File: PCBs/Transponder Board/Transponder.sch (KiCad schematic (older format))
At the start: 16 parts

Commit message: fixed swapped pins
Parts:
- added U?: PI4ULS5V201TAEX, symbol PI4ULS5V201TAEX
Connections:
- net XBEE-DIN: now also A?.1 (D0/TX)
- net XBEE-DOUT: now also U?.6 (B)
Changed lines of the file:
@@
+	1    0    0    -1
+$EndComp
+Text GLabel 4050 2650 2    60   Input ~ 0
+XBEE-DIN
+Text GLabel 6400 2950 2    60   Input ~ 0
+XBEE-DOUT
+$Comp
+L PI4ULS5V201TAEX U?
+U 1 1 5AB6D5A2
+P 5950 3100
+F 0 "U?" H 5950 3650 60  0000 C CNN
+F 1 "PI4ULS5V201TAEX" H 5950 3000 60  0000 C CNN
+F 2 "" H 5950 3100 60  0001 C CNN
+F 3 "" H 5950 3100 60  0001 C CNN
+	1    5950 3100
 	1    0    0    -1
 $EndComp

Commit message: transponder board
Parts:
- added J?: Conn_01x09, symbol Conn_01x09
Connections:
- net 5V: now also U?.1 (VccA), J?.2 (Pin_2)
- net D2: now also A?.9 (D6); no longer A?.5 (D2)
- net D3: now also A?.10 (D7); no longer A?.6 (D3)
- net D4: now also A?.11 (D8); no longer A?.7 (D4)
- net GND: now also U?.4 (GND), J?.1 (Pin_1), J?.4 (Pin_4)
- net MISO: now also J?.3 (Pin_3)
- net MOSI: now also J?.5 (Pin_5)
- net at A?.2 (D1/RX): now also U?.2 (A)
- net LCD_D4: now reaches A?.8 (D5)
- net LCD_D4: now also J?.6 (Pin_6)
- net 3.3V: now reaches C2.1, U?.1 (Vcc), U?.3 (+Vout)
- net 3.3V: now also U?.5 (EN), U?.8 (VccB)
- new net LCD_D5: A?.7 (D4), J?.7 (Pin_7)
- new net LCD_D6: A?.6 (D3), J?.8 (Pin_8)
- new net LCD_D7: A?.5 (D2), J?.9 (Pin_9)
- no-connect marks 0 -> 2
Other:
- note added: "LCD Pin 1"
- note added: "LCD Pin 2"
- note added: "LCD pin 11"
- note added: "LCD pin 12"
- note added: "LCD pin 13"
- note added: "LCD pin 14"
- note added: "LCD pin 4"
- note added: "LCD pin 5"
- note added: "LCD pin 6"
- moved on the sheet: A?, C1, C2, R1, R2, R?, U?

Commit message: transponder board
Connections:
- net D2: now also A?.19 (AD0/D14); no longer A?.9 (D6)
- net D3: now also A?.20 (AD1/D15); no longer A?.10 (D7)
- net D4: now also A?.21 (AD2/D16); no longer A?.11 (D8)
- net MISO: no longer J?.3 (Pin_3)
- net MOSI: no longer J?.5 (Pin_5)
- new net LCD_H/L_EN: A?.9 (D6), J?.5 (Pin_5)
- new net LCD_H/L_RS: A?.10 (D7), J?.3 (Pin_3)
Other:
- moved on the sheet: R?
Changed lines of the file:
@@
 Text GLabel 1550 3250 2    60   Input ~ 0
 5V
-Text GLabel 3650 4600 2    60   Input ~ 0
+Text GLabel 3650 5400 2    60   Input ~ 0
 D2
-Text GLabel 3350 4700 2    60   Input ~ 0
+Text GLabel 3350 5500 2    60   Input ~ 0
 D3
-Text GLabel 3050 4800 2    60   Input ~ 0
+Text GLabel 3050 5600 2    60   Input ~ 0
 D4
 Text GLabel 1550 2500 2    60   Input ~ 0
@@
 L R R?
 U 1 1 5AA8AA2D
-P 3300 4850
-F 0 "R?" V 3400 4850 50  0000 C CNN
-F 1 "10k" V 3300 4850 50  0000 C CNN
-F 2 "" V 3230 4850 50  0001 C CNN
-F 3 "" H 3300 4850 50  0001 C CNN
-	1    3300 4850
+P 3300 5650
+F 0 "R?" V 3400 5650 50  0000 C CNN
+F 1 "10k" V 3300 5650 50  0000 C CNN
+F 2 "" V 3230 5650 50  0001 C CNN
+F 3 "" H 3300 5650 50  0001 C CNN
+	1    3300 5650
 	1    0    0    -1
 $EndComp
@@
 L R R?
 U 1 1 5AA8AB66
-P 3000 4950
-F 0 "R?" V 3100 4950 50  0000 C CNN
-F 1 "10k" V 3000 4950 50  0000 C CNN
-F 2 "" V 2930 4950 50  0001 C CNN
-F 3 "" H 3000 4950 50  0001 C CNN
-	1    3000 4950
+P 3000 5750
+F 0 "R?" V 3100 5750 50  0000 C CNN
+F 1 "10k" V 3000 5750 50  0000 C CNN
+F 2 "" V 2930 5750 50  0001 C CNN
+F 3 "" H 3000 5750 50  0001 C CNN
+	1    3000 5750
 	1    0    0    -1
 $EndComp
@@
 L R R?
 U 1 1 5AA8A8A4
-P 3600 4750
-F 0 "R?" V 3680 4750 50  0000 C CNN
-F 1 "10k" V 3600 4750 50  0000 C CNN
-F 2 "" V 3530 4750 50  0001 C CNN
-F 3 "" H 3600 4750 50  0001 C CNN
-	1    3600 4750
-	1    0    0    -1
-$EndComp
-Wire Wire Line
-	2600 4600 3600 4600
-Wire Wire Line
-	3600 4600 3650 4600
-Connection ~ 3600 4600
-Wire Wire Line
-	2600 4700 3300 4700
-Wire Wire Line
-	3300 4700 3350 4700
-Connection ~ 3300 4700
-Wire Wire Line
-	2600 4800 3000 4800
-Wire Wire Line
-	3000 4800 3050 4800
-Connection ~ 3000 4800
+P 3600 5550
+F 0 "R?" V 3680 5550 50  0000 C CNN
+F 1 "10k" V 3600 5550 50  0000 C CNN
+F 2 "" V 3530 5550 50  0001 C CNN
+F 3 "" H 3600 5550 50  0001 C CNN
+	1    3600 5550
+	1    0    0    -1
+$EndComp
+Wire Wire Line
+	2600 5400 3600 5400
+Wire Wire Line
+	3600 5400 3650 5400
+Connection ~ 3600 5400
+Wire Wire Line
+	2600 5500 3300 5500
+Wire Wire Line
+	3300 5500 3350 5500
+Connection ~ 3300 5500
+Wire Wire Line
+	2600 5600 3000 5600
+Wire Wire Line
+	3000 5600 3050 5600
+Connection ~ 3000 5600
 $Comp
 L GND #PWR?
 U 1 1 5AA8AFB2
-P 3000 5100
-F 0 "#PWR?" H 3000 4850 50  0001 C CNN
-F 1 "GND" H 3000 4950 50  0000 C CNN
-F 2 "" H 3000 5100 50  0001 C CNN
-F 3 "" H 3000 5100 50  0001 C CNN
-	1    3000 5100
+P 3000 5900
+F 0 "#PWR?" H 3000 5650 50  0001 C CNN
+F 1 "GND" H 3000 5750 50  0000 C CNN
+F 2 "" H 3000 5900 50  0001 C CNN
+F 3 "" H 3000 5900 50  0001 C CNN
+	1    3000 5900
 	1    0    0    -1
 $EndComp
@@
 L GND #PWR?
 U 1 1 5AA8AFED
-P 3300 5000
-F 0 "#PWR?" H 3300 4750 50  0001 C CNN
-F 1 "GND" H 3300 4850 50  0000 C CNN
-F 2 "" H 3300 5000 50  0001 C CNN
-F 3 "" H 3300 5000 50  0001 C CNN
-	1    3300 5000
+P 3300 5800
+F 0 "#PWR?" H 3300 5550 50  0001 C CNN
+F 1 "GND" H 3300 5650 50  0000 C CNN
+F 2 "" H 3300 5800 50  0001 C CNN
+F 3 "" H 3300 5800 50  0001 C CNN
+	1    3300 5800
 	1    0    0    -1
 $EndComp
@@
 L GND #PWR?
 U 1 1 5AA8B028
-P 3600 4900
-F 0 "#PWR?" H 3600 4650 50  0001 C CNN
-F 1 "GND" H 3600 4750 50  0000 C CNN
-F 2 "" H 3600 4900 50  0001 C CNN
-F 3 "" H 3600 4900 50  0001 C CNN
-	1    3600 4900
+P 3600 5700
+F 0 "#PWR?" H 3600 5450 50  0001 C CNN
+F 1 "GND" H 3600 5550 50  0000 C CNN
+F 2 "" H 3600 5700 50  0001 C CNN
+F 3 "" H 3600 5700 50  0001 C CNN
+	1    3600 5700
 	1    0    0    -1
 $EndComp
@@
 L GND #PWR?
 U 1 1 5AB72A73
-P 5500 5900
-F 0 "#PWR?" H 5500 5650 50  0001 C CNN
-F 1 "GND" H 5500 5750 50  0000 C CNN
-F 2 "" H 5500 5900 50  0001 C CNN
-F 3 "" H 5500 5900 50  0001 C CNN
-	1    5500 5900
-	1    0    0    -1
-$EndComp
-Wire Wire Line
-	5500 5900 5500 5550
-Wire Wire Line
-	5500 5550 5950 5550
+P 5300 5900
+F 0 "#PWR?" H 5300 5650 50  0001 C CNN
+F 1 "GND" H 5300 5750 50  0000 C CNN
+F 2 "" H 5300 5900 50  0001 C CNN
+F 3 "" H 5300 5900 50  0001 C CNN
+	1    5300 5900
+	1    0    0    -1
+$EndComp
+Wire Wire Line
+	5300 5900 5300 5550
+Wire Wire Line
+	5300 5550 5950 5550
 Text GLabel 5950 5350 0    60   Input ~ 0
 LCD_D4
@@
 Text Notes 6750 5100 2    60   ~ 0
 LCD pin 14
-Text GLabel 5950 5450 0    60   Input ~ 0
-MOSI
-Text GLabel 5950 5650 0    60   Input ~ 0
-MISO
 Text GLabel 2600 4500 2    60   Input ~ 0
 LCD_D4
@@
 Text GLabel 2600 4200 2    60   Input ~ 0
 LCD_D7
+Text GLabel 5950 5450 0    60   Input ~ 0
+LCD_H/L_EN
+Text GLabel 5950 5650 0    60   Input ~ 0
+LCD_H/L_RS
+Text GLabel 2600 4600 2    60   Input ~ 0
+LCD_H/L_EN
+Text GLabel 2600 4700 2    60   Input ~ 0
+LCD_H/L_RS
 $EndSCHEMATC

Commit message: pinout changes
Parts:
- removed U?: PI4ULS5V201TAEX, symbol PI4ULS5V201TAEX
- added C?: 8.2pF, symbol C
- added C?: 1uF, symbol C
- added C?: 10uF, symbol C
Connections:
- net 3.3V: now also C?.1, C?.1, C?.1
- net GND: now also C?.2, C?.2, C?.2
- net shifter/A: now reaches A?.2 (D1/RX)
- net BATT+: no longer names the net of J?.1 (Pin_1), J?.2 (Pin_2)
- no-connect marks 2 -> 0
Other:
- note added: "Battery"
- note added: "Switch"
- moved on the sheet: J?, R1, R2, U?
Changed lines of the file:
@@
 $Descr A4 11693 8268
 encoding utf-8
-Sheet 1 1
+Sheet 1 2
 Title ""
 Date ""
@@
 L XBee-S2C U?
 U 1 1 5AA887F8
-P 6650 2200
-F 0 "U?" H 6550 3000 60  0000 C CNN
-F 1 "XBee-S2C" H 6650 1400 60  0000 C CNN
-F 2 "" H 6250 2150 60  0001 C CNN
-F 3 "" H 6250 2150 60  0001 C CNN
-	1    6650 2200
+P 9000 2250
+F 0 "U?" H 8900 3050 60  0000 C CNN
+F 1 "XBee-S2C" H 9000 1450 60  0000 C CNN
+F 2 "" H 8600 2200 60  0001 C CNN
+F 3 "" H 8600 2200 60  0001 C CNN
+	1    9000 2250
 	1    0    0    -1
 $EndComp
@@
 Wire Wire Line
 	5150 1350 5150 1250
-Text GLabel 5550 1850 0    60   Input ~ 0
+Text GLabel 7900 1900 0    60   Input ~ 0
 XBEE-DOUT
-Text GLabel 3950 2100 0    60   Input ~ 0
+Text GLabel 6050 2150 0    60   Input ~ 0
 XBEE-DIN
 $Comp
 L R R2
 U 1 1 5AA89647
-P 4100 2600
-F 0 "R2" V 4180 2600 50  0000 C CNN
-F 1 "2k" V 4100 2600 50  0000 C CNN
-F 2 "" V 4030 2600 50  0001 C CNN
-F 3 "" H 4100 2600 50  0001 C CNN
-	1    4100 2600
+P 6300 2650
+F 0 "R2" V 6380 2650 50  0000 C CNN
+F 1 "2k" V 6300 2650 50  0000 C CNN
+F 2 "" V 6230 2650 50  0001 C CNN
+F 3 "" H 6300 2650 50  0001 C CNN
+	1    6300 2650
 	1    0    0    -1
 $EndComp
@@
 L R R1
 U 1 1 5AA8967B
-P 4100 3200
-F 0 "R1" V 4180 3200 50  0000 C CNN
-F 1 "3k" V 4100 3200 50  0000 C CNN
-F 2 "" V 4030 3200 50  0001 C CNN
-F 3 "" H 4100 3200 50  0001 C CNN
-	1    4100 3200
-	1    0    0    -1
-$EndComp
-Wire Wire Line
-	3950 2100 4100 2100
-Wire Wire Line
-	4100 2100 4100 2450
-Wire Wire Line
-	4100 2750 4100 2900
-Wire Wire Line
-	4100 2900 4100 3050
-Wire Wire Line
-	4100 2900 4650 2900
-Wire Wire Line
-	4650 2900 4650 1950
-Wire Wire Line
-	4650 1950 5550 1950
-Connection ~ 4100 2900
+P 6300 3200
+F 0 "R1" V 6380 3200 50  0000 C CNN
+F 1 "3k" V 6300 3200 50  0000 C CNN
+F 2 "" V 6230 3200 50  0001 C CNN
+F 3 "" H 6300 3200 50  0001 C CNN
+	1    6300 3200
+	1    0    0    -1
+$EndComp
+Wire Wire Line
+	6050 2150 6300 2150
+Wire Wire Line
+	6300 2150 6300 2500
+Wire Wire Line
+	6300 2800 6300 2950
+Wire Wire Line
+	6300 2950 6300 3050
+Wire Wire Line
+	6300 2950 7700 2950
+Wire Wire Line
+	7700 2950 7700 2000
+Wire Wire Line
+	7700 2000 7900 2000
+Connection ~ 6300 2950
 $Comp
 L GND #PWR?
 U 1 1 5AA89745
-P 4100 3450
-F 0 "#PWR?" H 4100 3200 50  0001 C CNN
-F 1 "GND" H 4100 3300 50  0000 C CNN
-F 2 "" H 4100 3450 50  0001 C CNN
-F 3 "" H 4100 3450 50  0001 C CNN
-	1    4100 3450
-	1    0    0    -1
-$EndComp
-Wire Wire Line
-	4100 3450 4100 3350
+P 6300 3500
+F 0 "#PWR?" H 6300 3250 50  0001 C CNN
+F 1 "GND" H 6300 3350 50  0000 C CNN
+F 2 "" H 6300 3500 50  0001 C CNN
+F 3 "" H 6300 3500 50  0001 C CNN
+	1    6300 3500
+	1    0    0    -1
+$EndComp
+Wire Wire Line
+	6300 3500 6300 3350
 $Comp
 L GND #PWR?
 U 1 1 5AA897AD
-P 5450 2850
-F 0 "#PWR?" H 5450 2600 50  0001 C CNN
-F 1 "GND" H 5450 2700 50  0000 C CNN
-F 2 "" H 5450 2850 50  0001 C CNN
-F 3 "" H 5450 2850 50  0001 C CNN
-	1    5450 2850
-	1    0    0    -1
-$EndComp
-Wire Wire Line
-	5450 2850 5450 2650
-Wire Wire Line
-	5450 2650 5550 2650
-Text GLabel 1550 1950 2    60   Input ~ 0
+P 7800 2900
+F 0 "#PWR?" H 7800 2650 50  0001 C CNN
+F 1 "GND" H 7800 2750 50  0000 C CNN
+F 2 "" H 7800 2900 50  0001 C CNN
+F 3 "" H 7800 2900 50  0001 C CNN
+	1    7800 2900
+	1    0    0    -1
+$EndComp
+Wire Wire Line
+	7800 2900 7800 2700
+Wire Wire Line
+	7800 2700 7900 2700
+Text GLabel 1550 1700 2    60   Input ~ 0
 7.4V
-Text GLabel 1550 1850 2    60   Input ~ 0
-BATT+
-Text GLabel 1550 1100 2    60   Input ~ 0
-BATT+
 $Comp
 L GND #PWR?
@@
 L Conn_01x02 J?
 U 1 1 5AA8A05F
-P 1350 1950
-F 0 "J?" H 1350 2050 50  0000 C CNN
-F 1 "Conn_01x02" H 1350 1750 50  0000 C CNN
-F 2 "" H 1350 1950 50  0001 C CNN
-F 3 "" H 1350 1950 50  0001 C CNN
-	1    1350 1950
+P 1350 1700
+F 0 "J?" H 1350 1800 50  0000 C CNN
+F 1 "Conn_01x02" H 1350 1500 50  0000 C CNN
+F 2 "" H 1350 1700 50  0001 C CNN
+F 3 "" H 1350 1700 50  0001 C CNN
+	1    1350 1700
 	-1   0    0    1
 $EndComp
@@
 Text GLabel 2600 4000 2    60   Input ~ 0
 XBEE-DIN
-Text GLabel 4950 4200 2    60   Input ~ 0
-XBEE-DOUT
-$Comp
-L PI4ULS5V201TAEX U?
-U 1 1 5AB6D5A2
-P 4500 4350
-F 0 "U?" H 4500 4900 60  0000 C CNN
-F 1 "PI4ULS5V201TAEX" H 4500 4250 60  0000 C CNN
-F 2 "" H 4500 4350 60  0001 C CNN
-F 3 "" H 4500 4350 60  0001 C CNN
-	1    4500 4350
-	1    0    0    -1
-$EndComp
 Text GLabel 5500 900  2    60   Input ~ 0
 3.3V
@@
 Wire Wire Line
 	5150 900  5500 900
-Text GLabel 5550 1750 0    60   Input ~ 0
+Text GLabel 6400 1800 0    60   Input ~ 0
 3.3V
-Text GLabel 4950 4000 2    60   Input ~ 0
-3.3V
-Text GLabel 4950 4300 2    60   Input ~ 0
-3.3V
-Wire Wire Line
-	2600 4100 4050 4100
-Text GLabel 4050 4000 0    60   Input ~ 0
-5V
-$Comp
-L GND #PWR?
-U 1 1 5AB70428
-P 3950 4400
-F 0 "#PWR?" H 3950 4150 50  0001 C CNN
-F 1 "GND" H 3950 4250 50  0000 C CNN
-F 2 "" H 3950 4400 50  0001 C CNN
-F 3 "" H 3950 4400 50  0001 C CNN
-	1    3950 4400
-	1    0    0    -1
-$EndComp
-Wire Wire Line
-	3950 4400 3950 4300
-Wire Wire Line
-	3950 4300 4050 4300
-NoConn ~ 4950 4100
-NoConn ~ 4050 4200
 $Comp
 L Conn_01x09 J?
@@
 Text GLabel 2600 4700 2    60   Input ~ 0
 LCD_H/L_RS
+Wire Wire Line
+	1550 1100 1750 1100
+Wire Wire Line
+	1750 1100 1750 1600
+Wire Wire Line
+	1750 1600 1550 1600
+Text Notes 950  1100 0    60   ~ 0
+Battery
+Text Notes 950  1700 0    60   ~ 0
+Switch
+$Comp
+L C C?
+U 1 1 5AB9BB4C
+P 7150 2000
+F 0 "C?" H 7175 2100 50  0000 L CNN
+F 1 "8.2pF" H 7175 1900 50  0000 L CNN
+F 2 "" H 7188 1850 50  0001 C CNN
+F 3 "" H 7150 2000 50  0001 C CNN
+	1    7150 2000
+	1    0    0    -1
+$EndComp
+$Comp
+L C C?
+U 1 1 5AB9BC07
+P 6850 2000
+F 0 "C?" H 6875 2100 50  0000 L CNN
+F 1 "1uF" H 6875 1900 50  0000 L CNN
+F 2 "" H 6888 1850 50  0001 C CNN
+F 3 "" H 6850 2000 50  0001 C CNN
+	1    6850 2000
+	1    0    0    -1
+$EndComp
+$Comp
+L C C?
+U 1 1 5AB9BC5D
+P 6550 2000
+F 0 "C?" H 6575 2100 50  0000 L CNN
+F 1 "10uF" H 6575 1900 50  0000 L CNN
+F 2 "" H 6588 1850 50  0001 C CNN
+F 3 "" H 6550 2000 50  0001 C CNN
+	1    6550 2000
+	1    0    0    -1
+$EndComp
+Wire Wire Line
+	6400 1800 6550 1800
+Wire Wire Line
+	6550 1800 6850 1800
+Wire Wire Line
+	6850 1800 7150 1800
+Wire Wire Line
+	7150 1800 7900 1800
+Wire Wire Line
+	6550 1850 6550 1800
+Connection ~ 6550 1800
+Wire Wire Line
+	6850 1850 6850 1800
+Connection ~ 6850 1800
+Wire Wire Line
+	7150 1850 7150 1800
+Connection ~ 7150 1800
+$Comp
+L GND #PWR?
+U 1 1 5AB9C29E
+P 6550 2150
+F 0 "#PWR?" H 6550 1900 50  0001 C CNN
+F 1 "GND" H 6550 2000 50  0000 C CNN
+F 2 "" H 6550 2150 50  0001 C CNN
+F 3 "" H 6550 2150 50  0001 C CNN
+	1    6550 2150
+	1    0    0    -1
+$EndComp
+$Comp
+L GND #PWR?
+U 1 1 5AB9C2E8
+P 6850 2150
+F 0 "#PWR?" H 6850 1900 50  0001 C CNN
+F 1 "GND" H 6850 2000 50  0000 C CNN
+F 2 "" H 6850 2150 50  0001 C CNN
+F 3 "" H 6850 2150 50  0001 C CNN
+	1    6850 2150
+	1    0    0    -1
+$EndComp
+$Comp
+L GND #PWR?
+U 1 1 5AB9C332
+P 7150 2150
+F 0 "#PWR?" H 7150 1900 50  0001 C CNN
+F 1 "GND" H 7150 2000 50  0000 C CNN
+F 2 "" H 7150 2150 50  0001 C CNN
+F 3 "" H 7150 2150 50  0001 C CNN
+	1    7150 2150
+	1    0    0    -1
+$EndComp
+$Sheet
+S 3450 3850 700  350
+U 5AB9CB76
+F0 "shifter" 60
+F1 "shifter.sch" 60
+F2 "VccA" I L 3450 3950 60
+F3 "VccB" I R 4150 3950 60
+F4 "B" I R 4150 4100 60
+F5 "A" I L 3450 4100 60
+$EndSheet
+Text GLabel 3450 3950 0    60   Input ~ 0
+5V
+Text GLabel 4150 3950 2    60   Input ~ 0
+3.3V
+Text GLabel 4150 4100 2    60   Input ~ 0
+XBEE-DOUT
+Wire Wire Line
+	2600 4100 3450 4100
 $EndSCHEMATC

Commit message: Added BOM and software outline
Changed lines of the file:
@@
 $EndComp
 Wire Wire Line
-	1250 5950 1250 6050
-Wire Wire Line
-	1250 6050 1250 6250
+	1250 5950 1250 6250
 Connection ~ 1250 6050
 $Comp
@@
 	3550 950  3550 900
 Wire Wire Line
-	3300 900  3550 900
-Wire Wire Line
-	3550 900  3800 900
+	3300 900  3800 900
 Wire Wire Line
 	3550 1250 3550 1350
@@
 	6300 2150 6300 2500
 Wire Wire Line
-	6300 2800 6300 2950
-Wire Wire Line
-	6300 2950 6300 3050
+	6300 2800 6300 3050
 Wire Wire Line
 	6300 2950 7700 2950
@@
 $EndComp
 Wire Wire Line
-	2600 5400 3600 5400
-Wire Wire Line
-	3600 5400 3650 5400
+	2600 5400 3650 5400
 Connection ~ 3600 5400
 Wire Wire Line
-	2600 5500 3300 5500
-Wire Wire Line
-	3300 5500 3350 5500
+	2600 5500 3350 5500
 Connection ~ 3300 5500
 Wire Wire Line
-	2600 5600 3000 5600
-Wire Wire Line
-	3000 5600 3050 5600
+	2600 5600 3050 5600
 Connection ~ 3000 5600
 $Comp
@@
 3.3V
 Wire Wire Line
-	4900 900  5150 900
-Wire Wire Line
-	5150 900  5500 900
+	4900 900  5500 900
 Text GLabel 6400 1800 0    60   Input ~ 0
 3.3V
@@
 $EndComp
 Wire Wire Line
-	6400 1800 6550 1800
-Wire Wire Line
-	6550 1800 6850 1800
-Wire Wire Line
-	6850 1800 7150 1800
-Wire Wire Line
-	7150 1800 7900 1800
+	6400 1800 7900 1800
 Wire Wire Line
 	6550 1850 6550 1800

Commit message: completed layout for transponder board
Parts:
- A1: renamed from A?; footprint (none) -> arduino:Arduino_Nano
- C1, C2: footprint (none) -> Capacitors_SMD:C_0805_HandSoldering
- C3, C4, C5: renamed from C?; footprint (none) -> Capacitors_SMD:C_0805_HandSoldering
- J1, J2, J3, J4, J5: renamed from J?; footprint (none) -> molex:molex_kk_22-23-2021
- J6: renamed from J?; footprint (none) -> screwTerminals:VI0921550000G
- R1, R2: footprint (none) -> Resistors_SMD:R_0805_HandSoldering
- R3, R4, R5: renamed from R?; footprint (none) -> Resistors_SMD:R_0805_HandSoldering
- U1: renamed from U?; footprint (none) -> sip:SIP3Large
- U2: renamed from U?; footprint (none) -> adafruit:adafruit254
- U3: renamed from U?; footprint (none) -> SparkFun-RF:XBEE-1

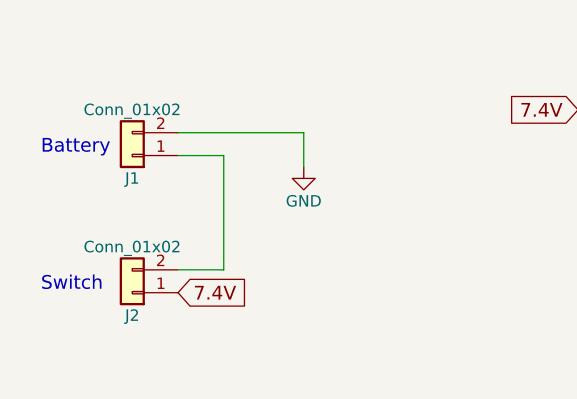
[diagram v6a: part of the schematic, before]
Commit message: rerouted payload instr board and completed all changes per Alexs review
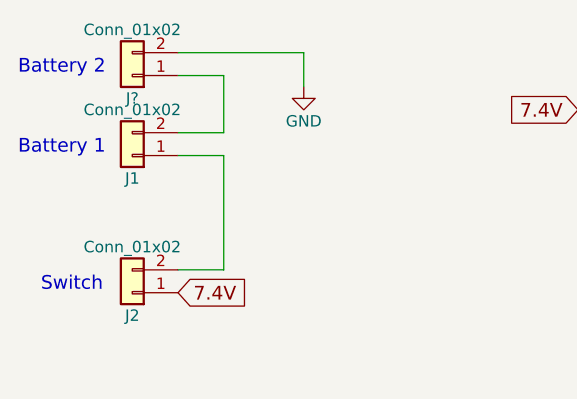
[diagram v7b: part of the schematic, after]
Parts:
- added J?: Conn_01x02, molex:molex_kk_22-23-2021, symbol Conn_01x02
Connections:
- net GND: now also J?.2 (Pin_2); no longer J1.2 (Pin_2)
- new net: J1.2 (Pin_2), J?.1 (Pin_1)
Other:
- note added: "Battery 1"
- note added: "Battery 2"
- note removed: "Battery"
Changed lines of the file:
@@
 L GND #PWR08
 U 1 1 5AA89F41
-P 2100 1150
-F 0 "#PWR08" H 2100 900 50  0001 C CNN
-F 1 "GND" H 2100 1000 50  0000 C CNN
-F 2 "" H 2100 1150 50  0001 C CNN
-F 3 "" H 2100 1150 50  0001 C CNN
-	1    2100 1150
+P 2100 800
+F 0 "#PWR08" H 2100 550 50  0001 C CNN
+F 1 "GND" H 2100 650 50  0000 C CNN
+F 2 "" H 2100 800 50  0001 C CNN
+F 3 "" H 2100 800 50  0001 C CNN
+	1    2100 800
 	1    0    0    -1
 $EndComp
@@
 $EndComp
 Wire Wire Line
-	1550 1000 2100 1000
-Wire Wire Line
-	2100 1000 2100 1150
+	1550 650  2100 650
+Wire Wire Line
+	2100 650  2100 800
 $Comp
 L Conn_01x02 J3
@@
 Wire Wire Line
 	1750 1600 1550 1600
-Text Notes 950  1100 0    60   ~ 0
-Battery
+Text Notes 850  1100 0    60   ~ 0
+Battery 1
 Text Notes 950  1700 0    60   ~ 0
 Switch
@@
 Wire Wire Line
 	2600 4100 3450 4100
+$Comp
+L Conn_01x02 J?
+U 1 1 5AC4138A
+P 1350 750
+F 0 "J?" H 1350 850 50  0000 C CNN
+F 1 "Conn_01x02" H 1350 550 50  0000 C CNN
+F 2 "molex:molex_kk_22-23-2021" H 1350 750 50  0001 C CNN
+F 3 "" H 1350 750 50  0001 C CNN
+	1    1350 750
+	-1   0    0    1
+$EndComp
+Text Notes 850  750  0    60   ~ 0
+Battery 2
+Wire Wire Line
+	1550 1000 1750 1000
+Wire Wire Line
+	1750 1000 1750 750
+Wire Wire Line
+	1750 750  1550 750
 $EndSCHEMATC

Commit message: transponder changes as per Alexs review
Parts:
- J1: footprint molex:molex_kk_22-23-2021 -> Connectors_JST:JST_PH_B2B-PH-K_02x2.00mm_Straight
- J7: renamed from J?; footprint molex:molex_kk_22-23-2021 -> Connectors_JST:JST_PH_B2B-PH-K_02x2.00mm_Straight
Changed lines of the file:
@@
 F 0 "J1" H 1350 1200 50  0000 C CNN
 F 1 "Conn_01x02" H 1350 900 50  0000 C CNN
-F 2 "molex:molex_kk_22-23-2021" H 1350 1100 50  0001 C CNN
+F 2 "Connectors_JST:JST_PH_B2B-PH-K_02x2.00mm_Straight" H 1350 1100 50  0001 C CNN
 F 3 "" H 1350 1100 50  0001 C CNN
 	1    1350 1100
@@
 	2600 4100 3450 4100
 $Comp
-L Conn_01x02 J?
+L Conn_01x02 J7
 U 1 1 5AC4138A
 P 1350 750
-F 0 "J?" H 1350 850 50  0000 C CNN
+F 0 "J7" H 1350 850 50  0000 C CNN
 F 1 "Conn_01x02" H 1350 550 50  0000 C CNN
-F 2 "molex:molex_kk_22-23-2021" H 1350 750 50  0001 C CNN
+F 2 "Connectors_JST:JST_PH_B2B-PH-K_02x2.00mm_Straight" H 1350 750 50  0001 C CNN
 F 3 "" H 1350 750 50  0001 C CNN
 	1    1350 750
